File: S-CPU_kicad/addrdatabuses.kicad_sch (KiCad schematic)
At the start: 168 parts

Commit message: Big update on the hierarchical sheet. DMA section update too.
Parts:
- removed QKEL0, QKEL1, QKEL2, QKEL3, QKQM0, QKQM1, QKQM2, QKQM3, RKOE0, RKOE1, RKOE2, RKOE3, RKUL0, RKUL1, RKUL2, RKUL3: TRI_BUF_IF1, symbol Ricoh_Cells:TRI_BUF_IF1
- removed QKGG, QKLR, RKPQ, RKPR, RKRK: INVERTER_A, symbol Ricoh_Cells:INVERTER_A
- removed QKHU, RKQY: NAND_3, symbol Ricoh_Cells:NAND_3
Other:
- note removed: "B-BUS"
- note removed: "B_BUS Address coming from DMA banks during DMA or from A bus otherwise"

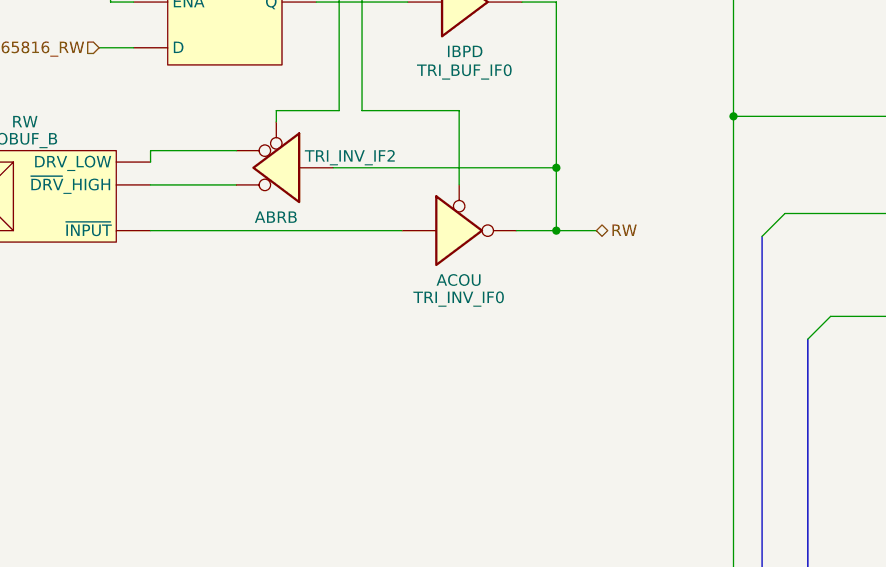
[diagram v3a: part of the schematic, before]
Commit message: DMA section update. Found errors between some MUX and MUXI gates.
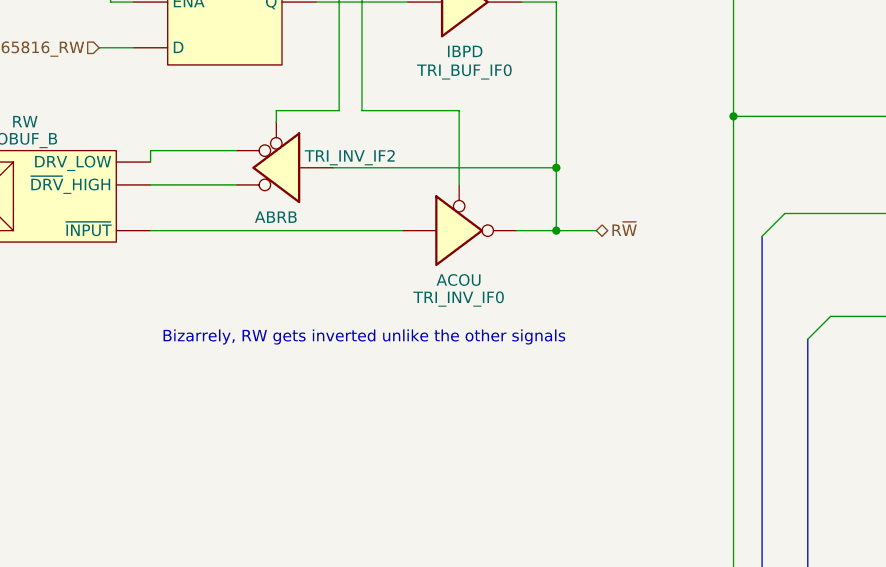
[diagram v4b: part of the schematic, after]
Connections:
- net RW renamed R~{W}
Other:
- note added: "Bizarrely, RW gets inverted unlike the other signals"
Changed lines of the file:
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@@
     (effects (font (size 5 5) (thickness 1) bold) (justify left bottom))
+  )
+  (text "Bizarrely, RW gets inverted unlike the other signals"
+    (at 149.225 107.95 0)
+    (effects (font (size 1.27 1.27)) (justify left bottom))
   )
   (label "A22" (at 334.01 168.275 180) (fields_autoplaced)
@@
     (effects (font (size 1.27 1.27)) (justify right))
   )
-  (hierarchical_label "RW" (shape tri_state) (at 197.485 95.25 0) (fields_autoplaced)
+  (hierarchical_label "R~{W}" (shape tri_state) (at 197.485 95.25 0) (fields_autoplaced)
     (effects (font (size 1.27 1.27)) (justify left))
   )
